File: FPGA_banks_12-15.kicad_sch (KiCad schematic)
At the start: 2 parts

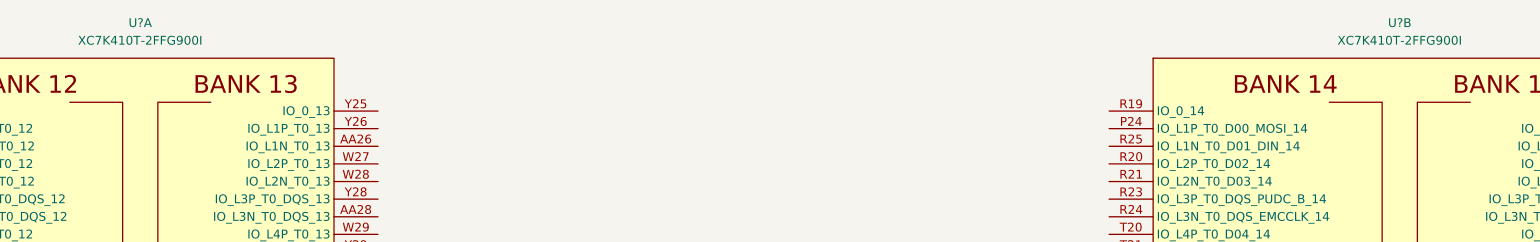
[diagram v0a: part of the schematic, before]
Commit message: Add MT41K512M8DA DDR3L
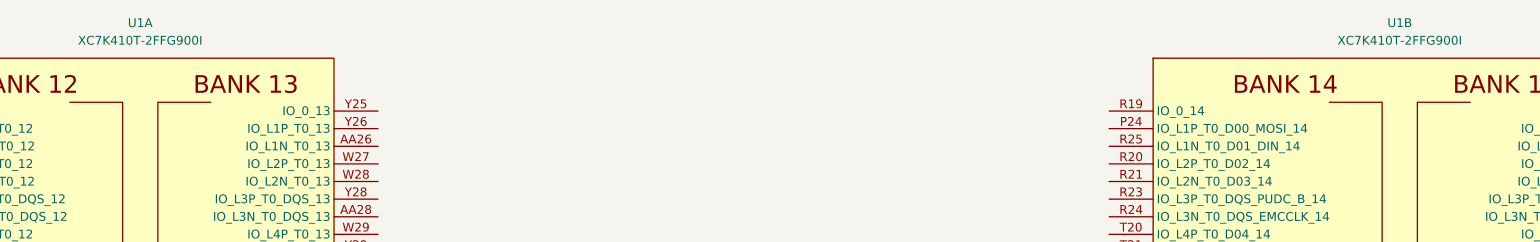
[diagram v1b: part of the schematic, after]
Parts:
- gave numbers to parts that had none: 1
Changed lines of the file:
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@@
   (symbol (lib_id "antmicroMicrocontrollers:XC7K410T-2FFG900I") (at 115.57 137.16 0) (unit 1)
     (in_bom yes) (on_board yes) (fields_autoplaced)
-    (property "Reference" "U?" (id 0) (at 115.57 63.5 0))
+    (property "Reference" "U1" (id 0) (at 115.57 63.5 0))
     (property "Value" "XC7K410T-2FFG900I" (id 1) (at 115.57 66.04 0))
     (property "Footprint" "antmicro-footprints:xc7k410t-2ffg900I" (id 2) (at 115.57 212.09 0)
@@
   (symbol (lib_id "antmicroMicrocontrollers:XC7K410T-2FFG900I") (at 297.18 137.16 0) (unit 2)
     (in_bom yes) (on_board yes) (fields_autoplaced)
-    (property "Reference" "U?" (id 0) (at 297.18 63.5 0))
+    (property "Reference" "U1" (id 0) (at 297.18 63.5 0))
     (property "Value" "XC7K410T-2FFG900I" (id 1) (at 297.18 66.04 0))
     (property "Footprint" "antmicro-footprints:xc7k410t-2ffg900I" (id 2) (at 297.18 212.09 0)
